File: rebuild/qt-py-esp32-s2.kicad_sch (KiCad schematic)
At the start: 45 parts, among them Q1 BOOT0, Q2 reset, U1 AP2112K-3.3, X1 ANTENNA_FP, X6 USB TYPE C, Y1 40MHz

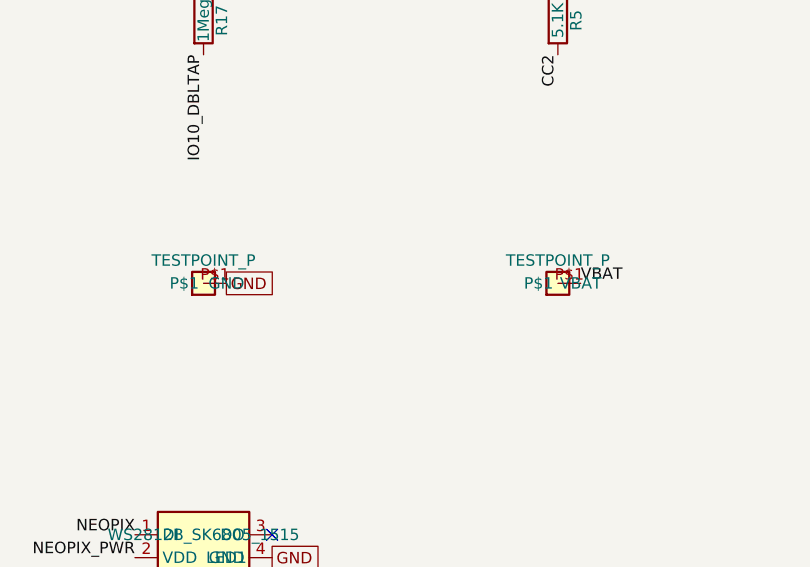
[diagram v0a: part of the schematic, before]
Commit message: gate3: PCB placement — 45/45 placed, 17.78x20.701 outline, DRC run
- qt-py footprint library extracted from the imported board (14 footprints)
- pad names preserved: A/A'/B/B', 1C..7C, A1B12/A4B9/A6/B6, MT1/MT2, C/A, 1/3, FP, P$1, TP
- create_board_from_schematic: 45 footprints, 34 nets, 159 pads assigned
- placement copied from the imported board: 45/45 exact x/y/rotation/layer
- outline 17.78 x 20.701 (8 Edge.Cuts segments), 2 fiducials, no frame
- Eagle rules: 6 mil clearance/width, 15.5 mil drill, 25% annulus, 0.254 edge, 2L 1.6mm
- fixed castellation pad rotation (importer stored 270/90): shorts 26 -> 2
- ERC footprint_link_issues 17 -> 0; annotation warning cleared via GND0/VBAT0
- DRC: 236 violations (37 errors, 199 warnings), 111 unconnected (unrouted)
- renders: 3D top/bottom, 2D
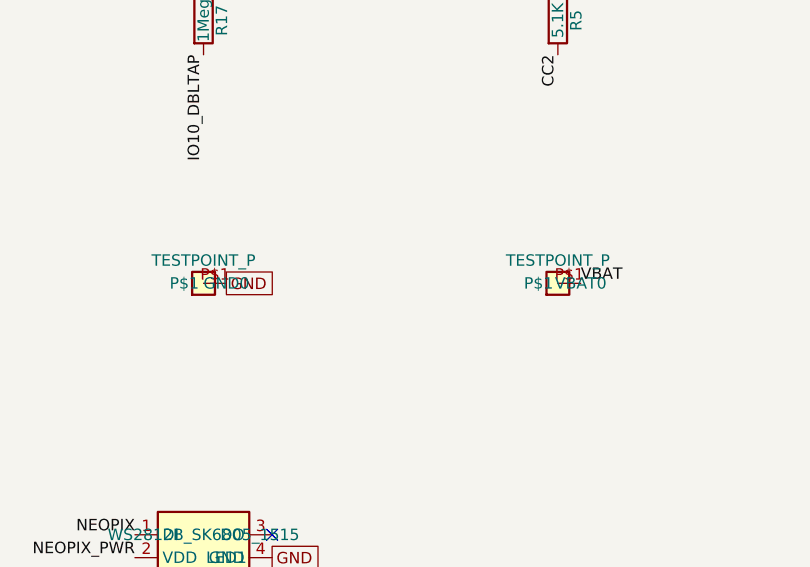
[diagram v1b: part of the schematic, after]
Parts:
- removed GND: TESTPOINT_P, qt-py:TESTPOINT_MINUS_1X3MM, symbol qt-py-esp32-s2:TESTPOINT_P
- removed VBAT: TESTPOINT_P, qt-py:TESTPOINT_PLUS_1X3MM, symbol qt-py-esp32-s2:TESTPOINT_P
- added GND0: TESTPOINT_P, qt-py:TESTPOINT_MINUS_1X3MM, symbol qt-py-esp32-s2:TESTPOINT_P
- added VBAT0: TESTPOINT_P, qt-py:TESTPOINT_PLUS_1X3MM, symbol qt-py-esp32-s2:TESTPOINT_P
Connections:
- net GND: now also GND0.P$1
- net VBAT: now also VBAT0.P$1

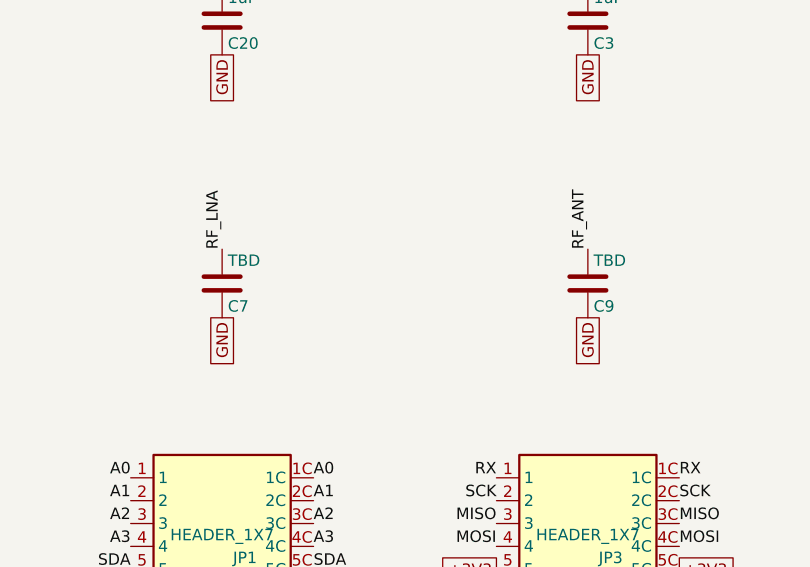
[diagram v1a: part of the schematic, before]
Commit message: gate4b/gate5: PASS as verified reconstruction; manufacturing outputs
- 4-layer source-faithful stack (In1 GND, In2 3.3V) approved; planes added
- reference zones restored; solid zone_connect on C15.2/C3.2/R6.1
- full reference signal routing fallback applied (approved)
- DRC 0 errors / 0 unconnected; D+ 9.238, D- 8.145, skew 1.093 mm
- C7/C9 marked DNP in schematic/board/BOM/PnP
- Gerbers (4 copper), PTH/NPTH drill, BOM, pos, stats, 2D/3D renders
- no fabrication, no ordering, no unconnected/DRC waivers
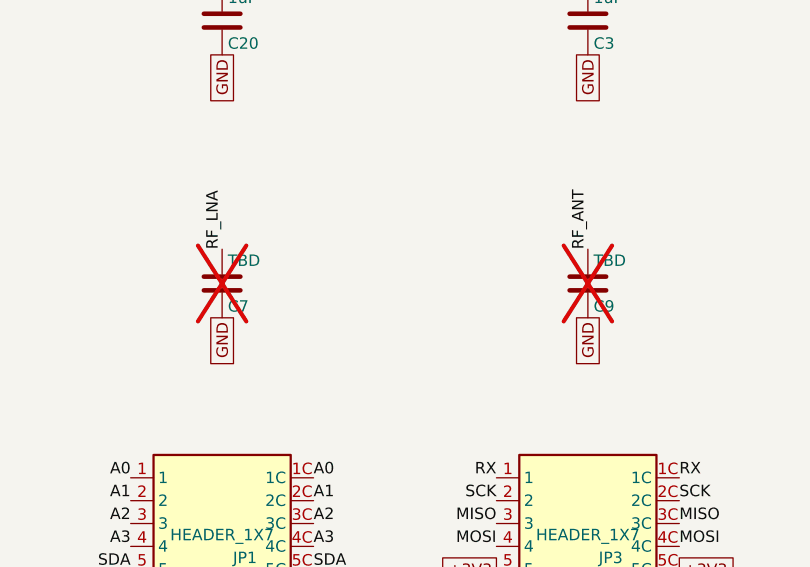
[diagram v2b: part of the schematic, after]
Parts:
- C7, C9: now not fitted
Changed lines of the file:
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@@
 		(on_board yes)
 		(in_pos_files yes)
-		(dnp no)
+		(dnp yes)
 		(property "Reference" "C7"
 			(at 70.485 121.92 0)
@@
 		(on_board yes)
 		(in_pos_files yes)
-		(dnp no)
+		(dnp yes)
 		(property "Reference" "C9"
 			(at 111.125 121.92 0)
